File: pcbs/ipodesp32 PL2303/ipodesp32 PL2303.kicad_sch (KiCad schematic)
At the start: 19 parts, among them IC1 PL2303SA__LF, IC2 3678, J1 USB_A, J2 Conn_01x19_Pin, U1 ESP32-DevKitC

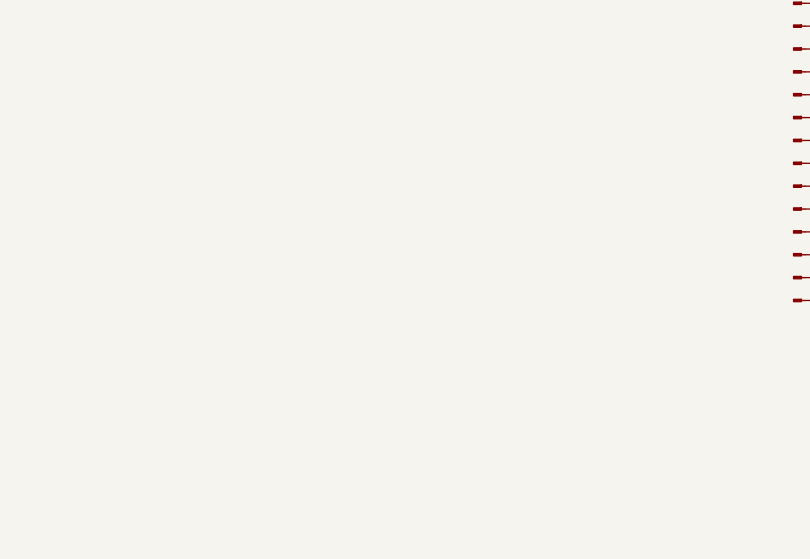
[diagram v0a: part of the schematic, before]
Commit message: Update to PCB with integrated PL2303
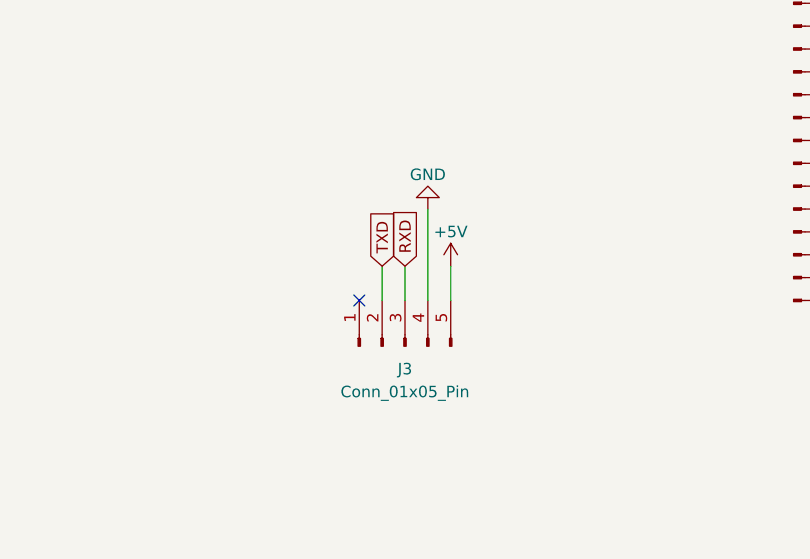
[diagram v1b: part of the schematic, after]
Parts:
- added J3: Conn_01x05_Pin, Connector_PinHeader_2.54mm:PinHeader_1x05_P2.54mm_Vertical, symbol Connector:Conn_01x05_Pin
- J2: now left out of the parts list
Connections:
- net +5V: now also J3.5 (Pin_5)
- net GND: now also J3.4 (Pin_4)
- net RXD: now also J3.3 (Pin_3)
- net TXD: now also J3.2 (Pin_2)
- no-connect marks 51 -> 52
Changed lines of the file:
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@@
   (no_connect (at 259.08 78.74))
   (no_connect (at 69.85 38.1))
+  (no_connect (at 115.57 120.65))
   (no_connect (at 259.08 121.92))
   (no_connect (at 69.85 27.94))
@@
     (stroke (width 0) (type default))
   )
+  (wire (pts (xy 125.73 116.84) (xy 125.73 120.65))
+    (stroke (width 0) (type default))
+  )
   (wire (pts (xy 163.83 21.59) (xy 163.83 24.13))
     (stroke (width 0) (type default))
   )
+  (wire (pts (xy 120.65 116.84) (xy 120.65 120.65))
+    (stroke (width 0) (type default))
+  )
   (wire (pts (xy 247.65 33.02) (xy 260.35 33.02))
     (stroke (width 0) (type default))
@@
     (stroke (width 0) (type default))
   )
+  (wire (pts (xy 123.19 110.49) (xy 123.19 120.65))
+    (stroke (width 0) (type default))
+  )
   (wire (pts (xy 185.42 29.21) (xy 185.42 33.02))
     (stroke (width 0) (type default))
@@
   )
   (wire (pts (xy 231.14 60.96) (xy 231.14 55.88))
+    (stroke (width 0) (type default))
+  )
+  (wire (pts (xy 118.11 116.84) (xy 118.11 120.65))
     (stroke (width 0) (type default))
   )
@@
     )
   )
+  (global_label "RXD" (shape input) (at 120.65 116.84 90) (fields_autoplaced)
+    (effects (font (size 1.27 1.27)) (justify left))
+    (property "Intersheetrefs" "${INTERSHEET_REFS}" (at 120.65 110.8389 90)
+      (effects (font (size 1.27 1.27)) (justify left) hide)
+    )
+  )
   (global_label "RXD" (shape input) (at 114.3 35.56 270) (fields_autoplaced)
     (effects (font (size 1.27 1.27)) (justify right))
@@
     )
   )
+  (global_label "TXD" (shape input) (at 118.11 116.84 90) (fields_autoplaced)
+    (effects (font (size 1.27 1.27)) (justify left))
+    (property "Intersheetrefs" "${INTERSHEET_REFS}" (at 118.11 111.1413 90)
+      (effects (font (size 1.27 1.27)) (justify left) hide)
+    )
+  )
   (symbol (lib_id "power:+3V3") (at 119.38 19.05 0) (unit 1)
     (in_bom yes) (on_board yes) (dnp no) (fields_autoplaced)
@@
     )
   )
+  (symbol (lib_id "power:+5V") (at 125.73 116.84 0) (unit 1)
+    (in_bom yes) (on_board yes) (dnp no) (fields_autoplaced)
+    (property "Reference" "#PWR027" (at 125.73 120.65 0)
+      (effects (font (size 1.27 1.27)) hide)
+    )
+    (property "Value" "+5V" (at 125.73 113.03 0)
+      (effects (font (size 1.27 1.27)))
+    )
+    (property "Footprint" "" (at 125.73 116.84 0)
+      (effects (font (size 1.27 1.27)) hide)
+    )
+    (property "Datasheet" "" (at 125.73 116.84 0)
+      (effects (font (size 1.27 1.27)) hide)
+    )
+    (pin "1")
+    (instances
+      (project "ipodesp32 PL2303"
+        (path "/de58fe00-6966-4192-80ec-79956931c145"
+          (reference "#PWR027") (unit 1)
+        )
+      )
+    )
+  )
   (symbol (lib_id "Connector:Conn_01x19_Pin") (at 163.83 97.79 0) (unit 1)
-    (in_bom yes) (on_board yes) (dnp no) (fields_autoplaced)
+    (in_bom no) (on_board yes) (dnp no) (fields_autoplaced)
     (property "Reference" "J2" (at 164.465 71.12 0)
       (effects (font (size 1.27 1.27)))
@@
     )
   )
+  (symbol (lib_id "Connector:Conn_01x05_Pin") (at 120.65 125.73 90) (unit 1)
+    (in_bom no) (on_board yes) (dnp no) (fields_autoplaced)
+    (property "Reference" "J3" (at 120.65 128.27 90)
+      (effects (font (size 1.27 1.27)))
+    )
+    (property "Value" "Conn_01x05_Pin" (at 120.65 130.81 90)
+      (effects (font (size 1.27 1.27)))
+    )
+    (property "Footprint" "Connector_PinHeader_2.54mm:PinHeader_1x05_P2.54mm_Vertical" (at 120.65 125.73 0)
+      (effects (font (size 1.27 1.27)) hide)
+    )
+    (property "Datasheet" "~" (at 120.65 125.73 0)
+      (effects (font (size 1.27 1.27)) hide)
+    )
+    (pin "1")
+    (pin "2")
+    (pin "3")
+    (pin "4")
+    (pin "5")
+    (instances
+      (project "ipodesp32 PL2303"
+        (path "/de58fe00-6966-4192-80ec-79956931c145"
+          (reference "J3") (unit 1)
+        )
+      )
+    )
+  )
   (symbol (lib_id "power:GND") (at 173.99 74.93 90) (unit 1)
     (in_bom yes) (on_board yes) (dnp no) (fields_autoplaced)
@@
         )
       )
+    )
+  )
+  (symbol (lib_id "power:GND") (at 123.19 110.49 180) (unit 1)
+    (in_bom yes) (on_board yes) (dnp no) (fields_autoplaced)
+    (property "Reference" "#PWR026" (at 123.19 104.14 0)
+      (effects (font (size 1.27 1.27)) hide)
+    )
+    (property "Value" "GND" (at 123.19 106.68 0)
+      (effects (font (size 1.27 1.27)))
+    )
+    (property "Footprint" "" (at 123.19 110.49 0)
+      (effects (font (size 1.27 1.27)) hide)
+    )
+    (property "Datasheet" "" (at 123.19 110.49 0)
+      (effects (font (size 1.27 1.27)) hide)
+    )
+    (pin "1")
+    (instances
+      (project "ipodesp32 PL2303"
+        (path "/de58fe00-6966-4192-80ec-79956931c145"
+          (reference "#PWR026") (unit 1)
+        )
+      )

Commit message: PCBWay Quote
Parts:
- C1: Manufacturer_Name (none) -> Samsung Electro-Mechanics; Manufacturer_Part_Number (none) -> CL10A475KP8NNNC
- C2: Manufacturer_Name (none) -> Yageo; Manufacturer_Part_Number (none) -> CC0603KRX7R7BB104
- C3: Manufacturer_Name (none) -> Kemet; Manufacturer_Part_Number (none) -> C0805C106K8PAC7800
- C4: Manufacturer_Name (none) -> Samsung Electro-Mechanics; Manufacturer_Part_Number (none) -> CL10B105KP8NNNC
- D1, D2, D3: value 2V -> 2.1V; Manufacturer_Name (none) -> Lite-On Inc.; Manufacturer_Part_Number (none) -> LTST-C190GKT
- IC1: value PL2303SA__LF -> PL2303GS; Manufacturer_Part_Number PL2303SA LF -> PL2303GS
- IC2: Mouser Part Number 485-3678 -> (none); Mouser Price/Stock https://www.mouser.co.uk/ProductDetail/Adafruit/3678?qs=W0y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 -> (none)
- J1: Manufacturer_Name (none) -> CNC Tech; Manufacturer_Part_Number (none) -> 1001-011-01101
- JP1, JP2, U1: now left out of the parts list
- R2, R3, R4: Manufacturer_Name (none) -> Yageo; Manufacturer_Part_Number (none) -> RC0603FR-071KL
- R5, R6: Manufacturer_Name (none) -> Yageo; Manufacturer_Part_Number (none) -> RC0603FR-0722RL
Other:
- company: (none) -> (c) Martin Roger
- title: (none) -> iPod ESP32 barebones PCB

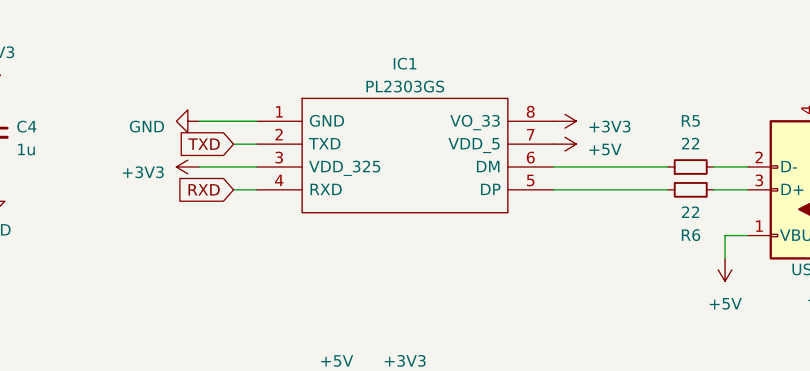
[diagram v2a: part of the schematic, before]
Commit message: Corrected GS to GL on PL2303
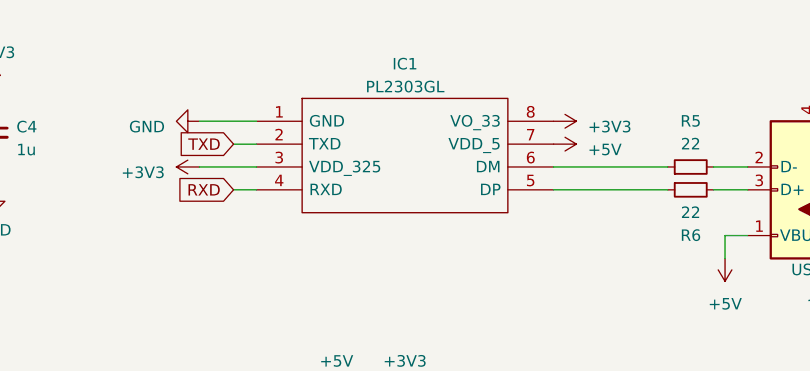
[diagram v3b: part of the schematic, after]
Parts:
- IC1: value PL2303GS -> PL2303GL
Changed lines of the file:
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@@
   (title_block
     (title "iPod ESP32 barebones PCB")
-    (date "2024-06-04")
-    (rev "0.2.0")
+    (date "2024-07-16")
+    (rev "0.2.1")
     (company "(c) Martin Roger")
   )
@@
       (effects (font (size 1.27 1.27)))
     )
-    (property "Value" "PL2303GS" (at 231.14 21.59 0)
-      (effects (font (size 1.27 1.27)))
-    )
+    (property "Value" "PL2303GL" (at 231.14 21.59 0)
+      (effects (font (size 1.27 1.27)))
+    )
